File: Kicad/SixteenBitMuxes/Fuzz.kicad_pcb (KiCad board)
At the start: 2 copper layers, 100 x 82 mm, 110 parts, among them J1 Audio In/Out JST XH, J10 Key Pad JST XH, J11 LCD JST XH, J12 Bypass Switch JST XH, J2 POT B10K JST XH, J3 POT B5K JST XH, J4 VOL POT A100K JST XH, J5 PowerTest_PinHeader, J6 9V Power JST XH, J7 Boot Reset PinHeader, J9 SWD_PinHeader, Q1 PN2222A, Q10 2SC1815, Q11 PN2222A, Q12 S9013, Q13 MMBT3904, Q14 S9018, Q15 BC848B, Q16 2SC1623, Q17 MPSA18, Q18 MMBT5551L, Q19 2N5088, Q2 MMBT3904, Q20 MMBTA42, Q21 BC807, Q22 BC846, Q23 BC847B, Q24 BC847C, Q25 BC848B, Q26 S9013, Q27 S9018, Q28 C945, Q29 2SC1623, Q3 MMBT5551L, Q30 2SC1815, Q31 MPSA18, Q32 2N5088, Q4 MMBTA42, Q5 BC807, Q6 BC846, Q7 BC847B, Q8 BC847C, Q9 C945, U1 AMS1117-5.0, U2 AMS1117-3.3, U21 CD4051B, U22 4504, U23 4504, U24 4504, U25 CD4053B, U3 STM32F103C8Tx, U4 CD4051B, U6 CD4067BM, U7 CD4067BM, U8 CD4067BM, U9 CD4067BM, Y1 8MHz

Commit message: PCB mostly
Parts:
- removed J3: POT B5K JST XH, Connector_JST:JST_XH_B2B-XH-A_1x02_P2.50mm_Vertical
- removed REF**: KiCad-Logo2_30mm_SilkScreen, Symbol:KiCad-Logo2_30mm_SilkScreen
- C3, C4: footprint Capacitor_THT:CP_Radial_D5.0mm_P2.50mm -> Diode_SMD:D_SMB_Handsoldering; moved to B.Cu
- D2: moved to B.Cu
- J10: value Key Pad JST XH -> JST XH Buttons; footprint Connector_JST:JST_XH_B8B-XH-A_1x08_P2.50mm_Vertical -> Connector_JST:JST_XH_B6B-XH-A_1x06_P2.50mm_Vertical
- J2: value POT B10K JST XH -> TONE_POTS; footprint Connector_JST:JST_XH_B2B-XH-A_1x02_P2.50mm_Vertical -> Connector_JST:JST_XH_B4B-XH-A_1x04_P2.50mm_Vertical
- R4: moved to F.Cu
- R5, R6, R7, R8: value 1K -> 10K; moved to B.Cu
- moved J10 70.5 mm to (55.5, 34.0), turned to 0 degrees
- moved R5 69.1 mm to (61.5, 41.3), turned to 270 degrees
- moved R6 66.9 mm to (64.8, 41.3), turned to 270 degrees
- moved R8 64.9 mm to (75.8, 41.3), turned to 90 degrees
- moved R7 64.9 mm to (68.1, 41.3), turned to 270 degrees
- moved J1 28.5 mm to (111.8, 34.0)
- moved J2 23.7 mm to (84.9, 34.0)
- moved J9 20.8 mm to (33.6, 68.5)
- moved J11 19.7 mm to (40.8, 34.0)
- moved D1 18.7 mm to (39.7, 54.2)
- moved R4 16.3 mm to (39.7, 49.0)
- moved J7 9.20 mm to (33.6, 81.4)
- moved J5 8.48 mm to (33.6, 51.5)
- moved D2 7.95 mm to (49.5, 42.0), turned to 270 degrees
- moved C3 6.62 mm to (41.2, 41.9), turned to 90 degrees
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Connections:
- J1 pad 1: GND -> GNDA
- J1 pad 3: GND -> GNDA
- J10 pad 1: Net-(J10-Pad1) -> +3V3
- J10 pad 2: Net-(J10-Pad2) -> /Mcu/GPIO_BUTTON_DECREASE
- J10 pad 3: Net-(J10-Pad3) -> +3V3
- J10 pad 4: Net-(J10-Pad4) -> /Mcu/GPIO_BUTTON_ENTER
- J10 pad 5: /Mcu/GPIO_KEYPAD_ROW_4 -> +3V3
- J10 pad 6: /Mcu/GPIO_KEYPAD_ROW_3 -> /Mcu/GPIO_BUTTON_INCREASE
- J2 pad 1: /TransistorsC/EMITTER -> /B10K
- Q11 pad 2: /TransistorsC/EMITTER -> /B10K
- Q13 pad 2: /TransistorsC/EMITTER -> /B10K
- Q18 pad 2: /TransistorsC/EMITTER -> /B10K
- Q20 pad 2: /TransistorsC/EMITTER -> /B10K
- Q21 pad 2: /TransistorsC/EMITTER -> /B10K
- Q22 pad 2: /TransistorsC/EMITTER -> /B10K
- Q23 pad 2: /TransistorsC/EMITTER -> /B10K
- Q24 pad 2: /TransistorsC/EMITTER -> /B10K
- Q25 pad 2: /TransistorsC/EMITTER -> /B10K
- Q26 pad 2: /TransistorsC/EMITTER -> /B10K
- Q27 pad 2: /TransistorsC/EMITTER -> /B10K
- Q28 pad 2: /TransistorsC/EMITTER -> /B10K
- Q29 pad 2: /TransistorsC/EMITTER -> /B10K
- Q30 pad 2: /TransistorsC/EMITTER -> /B10K
- Q31 pad 2: /TransistorsC/EMITTER -> /B10K
- Q32 pad 2: /TransistorsC/EMITTER -> /B10K
- R2 pad 1: /TransistorsC/EMITTER -> /B10K
- R5 pad 1: /Mcu/GPIO_KEYPAD_COLUMN_1 -> /Mcu/GPIO_BUTTON_DECREASE
- R5 pad 2: Net-(J10-Pad1) -> GND
- R6 pad 1: /Mcu/GPIO_KEYPAD_COLUMN_2 -> /Mcu/GPIO_BUTTON_ENTER
- R6 pad 2: Net-(J10-Pad2) -> GND
- R7 pad 1: /Mcu/GPIO_KEYPAD_COLUMN_3 -> /Mcu/GPIO_BUTTON_INCREASE
- R7 pad 2: Net-(J10-Pad3) -> GND
- R8 pad 1: /Mcu/GPIO_KEYPAD_COLUMN_4 -> GND
- R8 pad 2: Net-(J10-Pad4) -> /Mcu/BYPASS_SWITCH_3V3
- U22 pad 11: /TRANSISTOR_B_SELECTION_0_3V3 -> /CAPACITOR_A_SELECTION_0_3V3
- U22 pad 14: /TRANSISTOR_B_SELECTION_1_3V3 -> /CAPACITOR_A_SELECTION_1_3V3
- U22 pad 3: /CAPACITOR_A_SELECTION_0_3V3 -> /TRANSISTOR_B_SELECTION_0_3V3
- U22 pad 5: /CAPACITOR_A_SELECTION_1_3V3 -> /TRANSISTOR_B_SELECTION_1_3V3
- U3 pad 10: /Mcu/GPIO_KEYPAD_COLUMN_1 -> Net-(U3-Pad10)
- U3 pad 2: /Mcu/GPIO_KEYPAD_COLUMN_4 -> Net-(U3-Pad2)
- U3 pad 3: /Mcu/GPIO_KEYPAD_COLUMN_3 -> Net-(U3-Pad3)
- U3 pad 38: /Mcu/GPIO_KEYPAD_ROW_1 -> Net-(U3-Pad38)
- U3 pad 39: /Mcu/GPIO_KEYPAD_ROW_2 -> /Mcu/GPIO_BUTTON_DECREASE
- U3 pad 4: /Mcu/GPIO_KEYPAD_COLUMN_2 -> Net-(U3-Pad4)
- U3 pad 40: /Mcu/GPIO_KEYPAD_ROW_3 -> /Mcu/GPIO_BUTTON_ENTER
- U3 pad 41: /Mcu/GPIO_KEYPAD_ROW_4 -> /Mcu/GPIO_BUTTON_INCREASE
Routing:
- net /B10K: track 0.00 -> 231.3 mm, vias 0 -> 5
- net /TransistorsC/EMITTER: track 216.9 -> 0.00 mm, vias 5 -> 0
- net /Mcu/GPIO_BUTTON_INCREASE: track 0.00 -> 63.7 mm, vias 0 -> 2
- net /Mcu/GPIO_BUTTON_ENTER: track 0.00 -> 60.8 mm, vias 0 -> 2
- net GNDA: track 50.5 -> 107.2 mm, vias 10 -> 30
- net +9V: track 331.0 -> 274.4 mm, vias 18 -> 15
- net /Mcu/GPIO_BUTTON_DECREASE: track 0.00 -> 55.2 mm, vias 0 -> 2
- net GND: track 41.9 -> 89.0 mm, vias 33 -> 55
- net /Mcu/GPIO_KEYPAD_COLUMN_1: track 35.4 -> 0.00 mm
- net /AudioInOut/JACK_IN_SIGNAL: track 35.4 -> 68.3 mm, vias 3 -> 1
- net /AudioInOut/JACK_OUT_SIGNAL: track 43.4 -> 75.9 mm, vias 4 -> 1
- net /Mcu/GPIO_KEYPAD_COLUMN_2: track 31.4 -> 0.00 mm
- net /Mcu/GPIO_KEYPAD_ROW_4: track 29.3 -> 0.00 mm
- net /Mcu/GPIO_KEYPAD_COLUMN_3: track 28.6 -> 0.00 mm
- net /Mcu/GPIO_KEYPAD_ROW_3: track 27.5 -> 0.00 mm
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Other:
- board text added: "10K:OUT IN"
- board text added: "5K:OUT IN"
- board text added: "AUDIO SIGNALS"
- board text added: "BUTTONS"
- board text added: "BYPASS"
- board text added: "CAPACITOR BANK A"
- board text added: "CAPACITOR BANK D"
- board text added: "FUZZ"
- board text added: "GND INC GND ENT GND DEC"
- board text added: "GROUND"
- board text added: "GUITAR PEDAL FUZZ EFFECT 15K FUZZ V0.2"
- board text added: "LCD"
- board text added: "LEVEL SHIFTER"
- board text added: "LEVEL SHIFTERS"
- board text added: "MICRO CONTROLLER"
- board text added: "OSCILLATOR CAPACITORS"
- board text added: "OUT GND IN GND"
- board text added: "POWER LED"
- board text added: "SDA 5V GND SCL"
- board text added: "TONE POTS"
- board text added: "TRANSISTOR BANK B"
- board text added: "TRANSISTOR BANK B MULTIPLEXERS"
- board text added: "TRANSISTOR BANK C"
- board text added: "TRANSISTOR BANK C MULTIPLEXERS"
- board text added: "VOLTAGE REGULATOR"
- board text added: "VOLTAGE REGULATOR DIODES"
- board text added: "VOLUME POT"
- board text added: "©2020 MICHEL KEIJZERS"
- board text removed: "15K Fuzz, V0.1"
- board text removed: "B10K:OUT IN"
- board text removed: "B5K: OUT IN"
- board text removed: "Bypass"
- board text removed: "Capacitor Bank A"
- board text removed: "Capacitor Bank D"
- board text removed: "Fuzz"
- board text removed: "Ground"
- board text removed: "KEY PAD"
- board text removed: "Key Pad"
- board text removed: "Level Shifter"
- board text removed: "Level Shifters"
- board text removed: "Micro Controller"
- board text removed: "R1 R2 R3 R4 C1 C2 C3 C4"
- board text removed: "SDA 5V GND SCL:LCD"
- board text removed: "SIG→ GND SIG← GND"
- board text removed: "Transistor Bank B"
- board text removed: "Transistor Bank B Multiplexers"
- board text removed: "Transistor Bank C"
- board text removed: "Transistor Bank C Multiplexers"
- board text removed: "Voltage Regulation"
- board text removed: "©2020 Michel Keijzers"

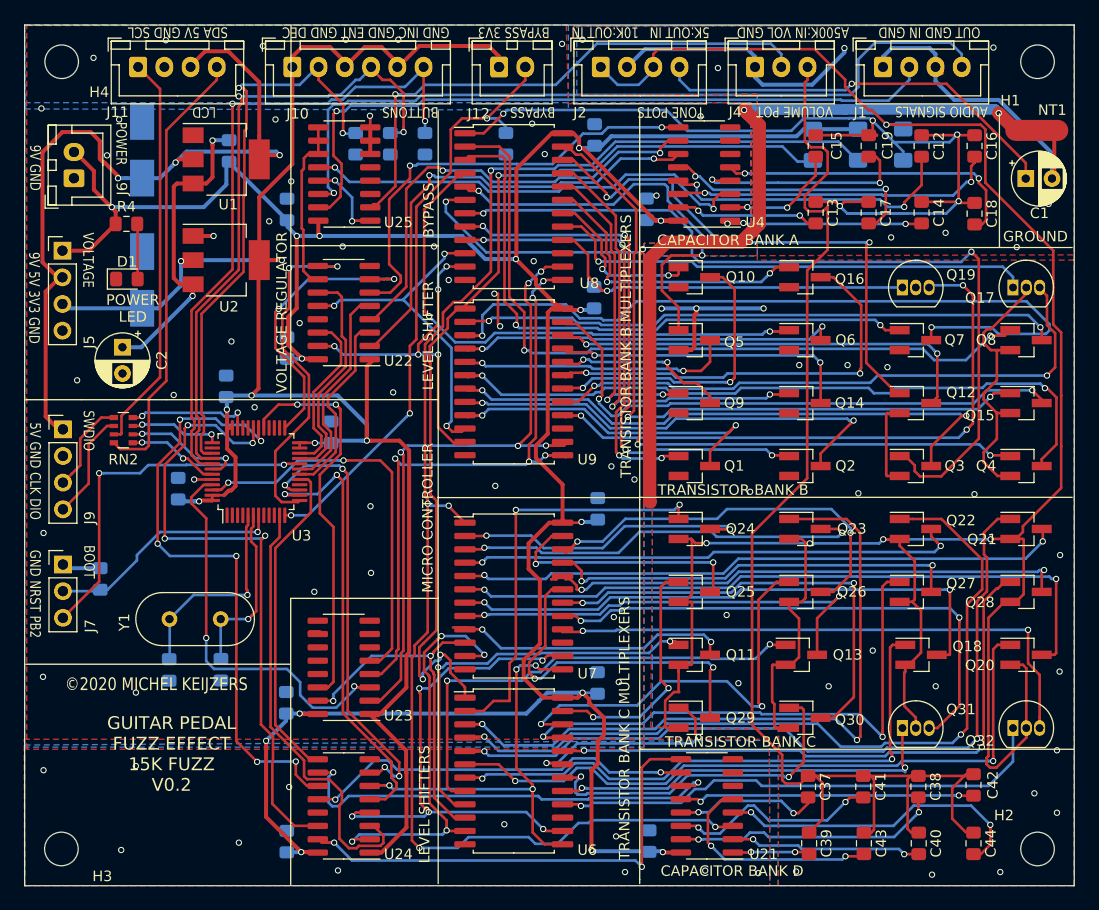
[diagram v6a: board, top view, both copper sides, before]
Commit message: Code + resistors
Many code changes (UI) + resistors -> pulldowns.
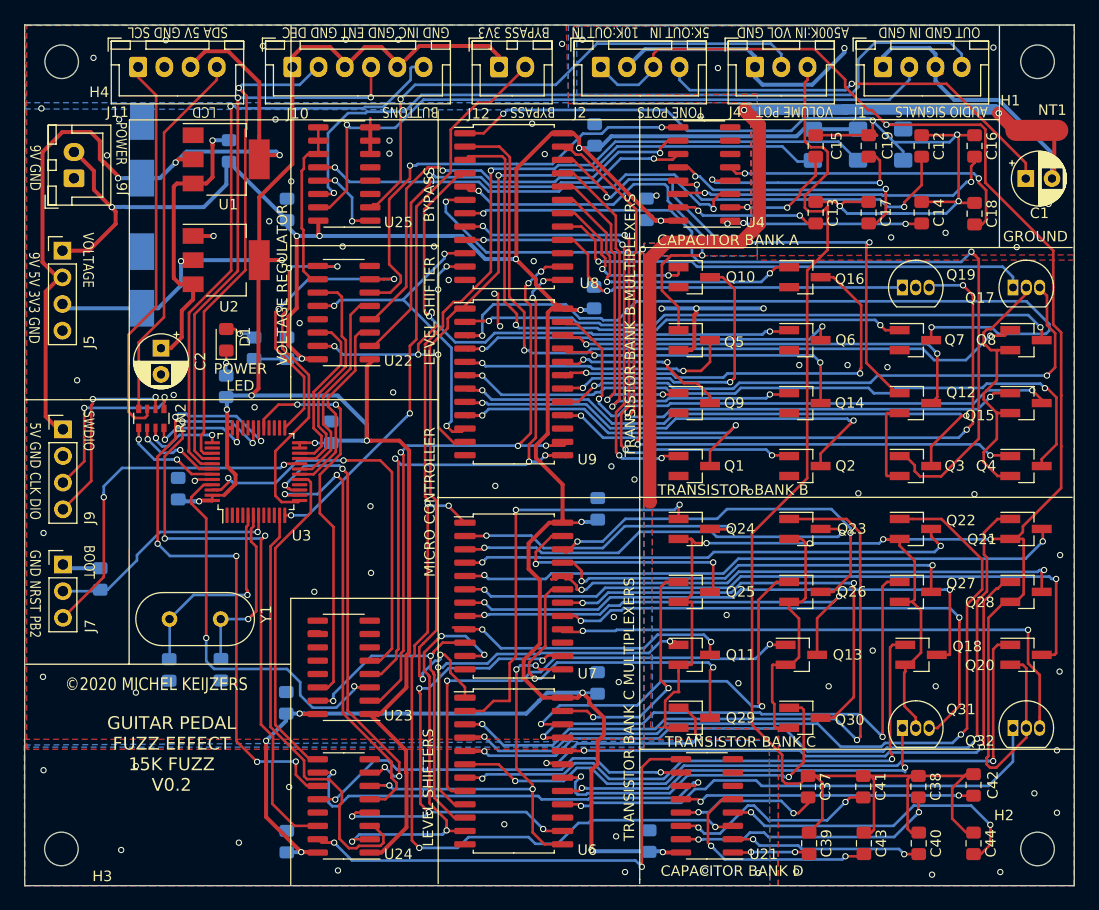
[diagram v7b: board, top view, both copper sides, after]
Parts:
- removed R5, R6, R7, R8: 10K, Resistor_SMD:R_0805_2012Metric_Pad1.15x1.40mm_HandSolder
- R4: moved to B.Cu
- moved R4 17.0 mm to (51.9, 60.8), turned to 90 degrees
- moved D1 11.1 mm to (49.2, 60.0), turned to 90 degrees
- moved C2 3.67 mm to (43.0, 60.8)
- moved RN2 2.90 mm to (42.1, 67.5), turned to 90 degrees
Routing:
- net /Mcu/GPIO_BUTTON_DECREASE: track 55.2 -> 46.2 mm, vias 2 -> 1
- net /Mcu/SYS_JTICK_SWCLK: track 10.3 -> 18.9 mm, vias 0 -> 2
- net /Mcu/SYS_JTMS_SWDIO: track 8.91 -> 17.4 mm, vias 0 -> 2
- net /Mcu/GPIO_BUTTON_ENTER: track 60.8 -> 52.9 mm
- net /Mcu/I2C1_SDA: track 42.5 -> 35.7 mm
- net /Mcu/GPIO_BUTTON_INCREASE: track 63.7 -> 58.2 mm, vias 2 -> 1
- net /Mcu/BYPASS_SWITCH_3V3: track 57.6 -> 54.2 mm, vias 3 -> 2
- net +9V: track 274.4 -> 277.7 mm
- net /Mcu/I2C1_SCL_MCU: track 11.9 -> 8.66 mm
- net Net-(D1-Pad2): track 5.27 -> 2.98 mm, vias 0 -> 1
- net GND: track 89.0 -> 91.1 mm, vias 55 -> 56
- net Net-(C2-Pad1): track 29.8 -> 27.9 mm, vias 2 -> 1
- net /AudioInOut/JACK_IN_SIGNAL: track 68.3 -> 66.5 mm
- net /Mcu/SYS_JTMS_SWDIO_MCU: track 11.9 -> 10.4 mm
- net /AudioInOut/JACK_OUT_SIGNAL: track 75.9 -> 74.6 mm
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
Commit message: Fixed store problem
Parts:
- moved C47 3.89 mm to (56.4, 64.4), turned to 270 degrees
- moved R4 3.75 mm to (52.8, 64.4), turned to 270 degrees
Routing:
- net Net-(D1-Pad2): track 2.98 -> 9.12 mm
- net +3V3: track 182.6 -> 179.1 mm, vias 7 -> 6
- net /CAPACITOR_A_SELECTION_2_3V3: track 27.5 -> 29.5 mm
- net +9V: track 277.7 -> 279.5 mm
- net /BYPASS_MODE_3V3: track 33.2 -> 34.7 mm
- net /TRANSISTOR_C_SELECTION_0_3V3: track 37.9 -> 39.0 mm
- net /CAPACITOR_A_SELECTION_1_3V3: track 16.2 -> 15.6 mm
- net /TRANSISTOR_B_SELECTION_0_3V3: track 18.2 -> 17.6 mm
- net /CAPACITOR_A_SELECTION_0_3V3: track 21.4 -> 20.7 mm
- net /TRANSISTOR_B_SELECTION_1_3V3: track 20.3 -> 19.7 mm
- net GND: track 91.1 -> 91.2 mm, vias 56 -> 55
